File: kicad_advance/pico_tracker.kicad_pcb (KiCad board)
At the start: 2 copper layers, 92.9 x 125.4 mm, 44 parts, among them J1 MIDI_OUT, J10 DclassAMP, J11 CODEC_DIG, J12 CODEC_ANA, J13 LINE_IN, J14 PHONES, J15 MIC_MODULE, J16 FUEL_GAUGE, J2 MIDI_IN, J3 MIDI_IN_A_B_VCC, J4 MIDI_IN_A_B_DATA, J5 MIDI_OUT_A_B_VCC, J6 MIDI_OUT_A_B_DATA, J7 DISPLAY, J8 SDCARD, J9 KILL_SWITCH, SW1 SW_PG1350, SW2 SW_PG1350, SW3 SW_PG1350, SW4 SW_PG1350, SW5 SW_PG1350, SW6 SW_PG1350, SW7 SW_PG1350, SW8 SW_PG1350, SW9 SW_PG1350, U1 Pico, U2 6N138

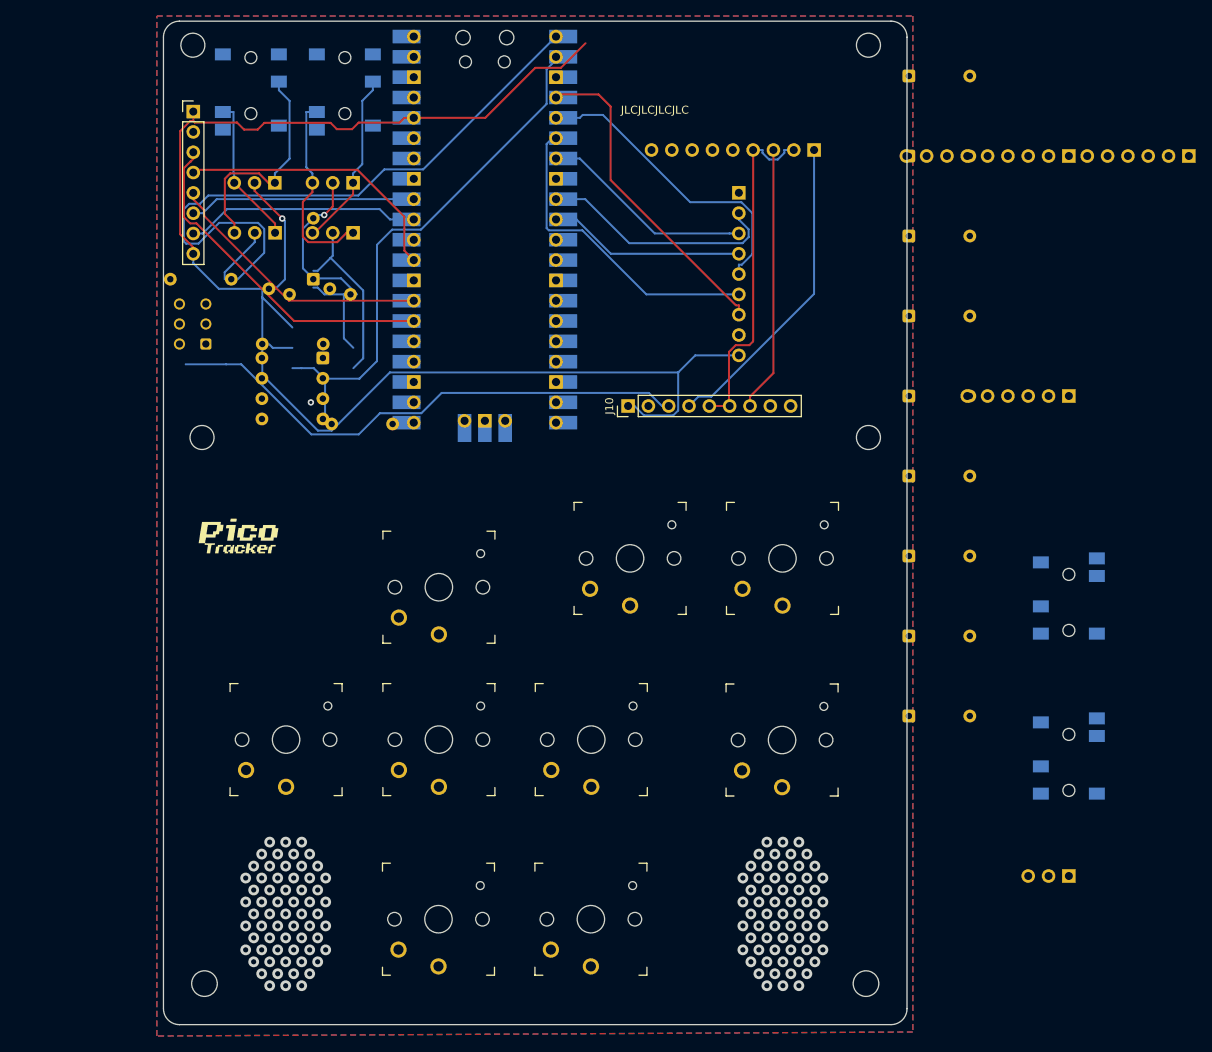
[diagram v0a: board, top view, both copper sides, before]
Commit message: Place and route the Advance-lite footprints in kicad_advance
Placement:
- All 9 matrix diodes (D2-D10) on B.Cu (back side), tucked among the
  switch rows with each cathode facing its ROW net
- Codec headers J11/J12, line-in J13, phones J14, mic J15, and
  fuel-gauge J16 placed on-board along the right edge

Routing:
- All 47 new-net connections auto-routed on a 0.2mm grid (0.25mm
  tracks, 0.25mm clearance, vias where a layer change is needed):
  COL0-2/ROW0-2 key matrix, I2S BCK/LRCK/DIN/data-in, codec MCLK,
  I2C SDA/SCL, MIC_IN, HP-amp L_AMP/R_AMP/AGND, header VCC/GND
- GND islands stitched to the pour; zones refilled

Verification:
- Total DRC count drops 528 -> 343 (refill cleared stale-fill shorts)
- No new violations on any new net; the lone new-net DRC flag
  (I2S_SDIN/VCC at U1.21/R4.2) already exists pre-routing in the
  dense MIDI/power cluster and is not caused by this work
- Switch positions, key layout, display, and MIDI jacks unchanged

Plan status section updated to reflect placed+routed state.
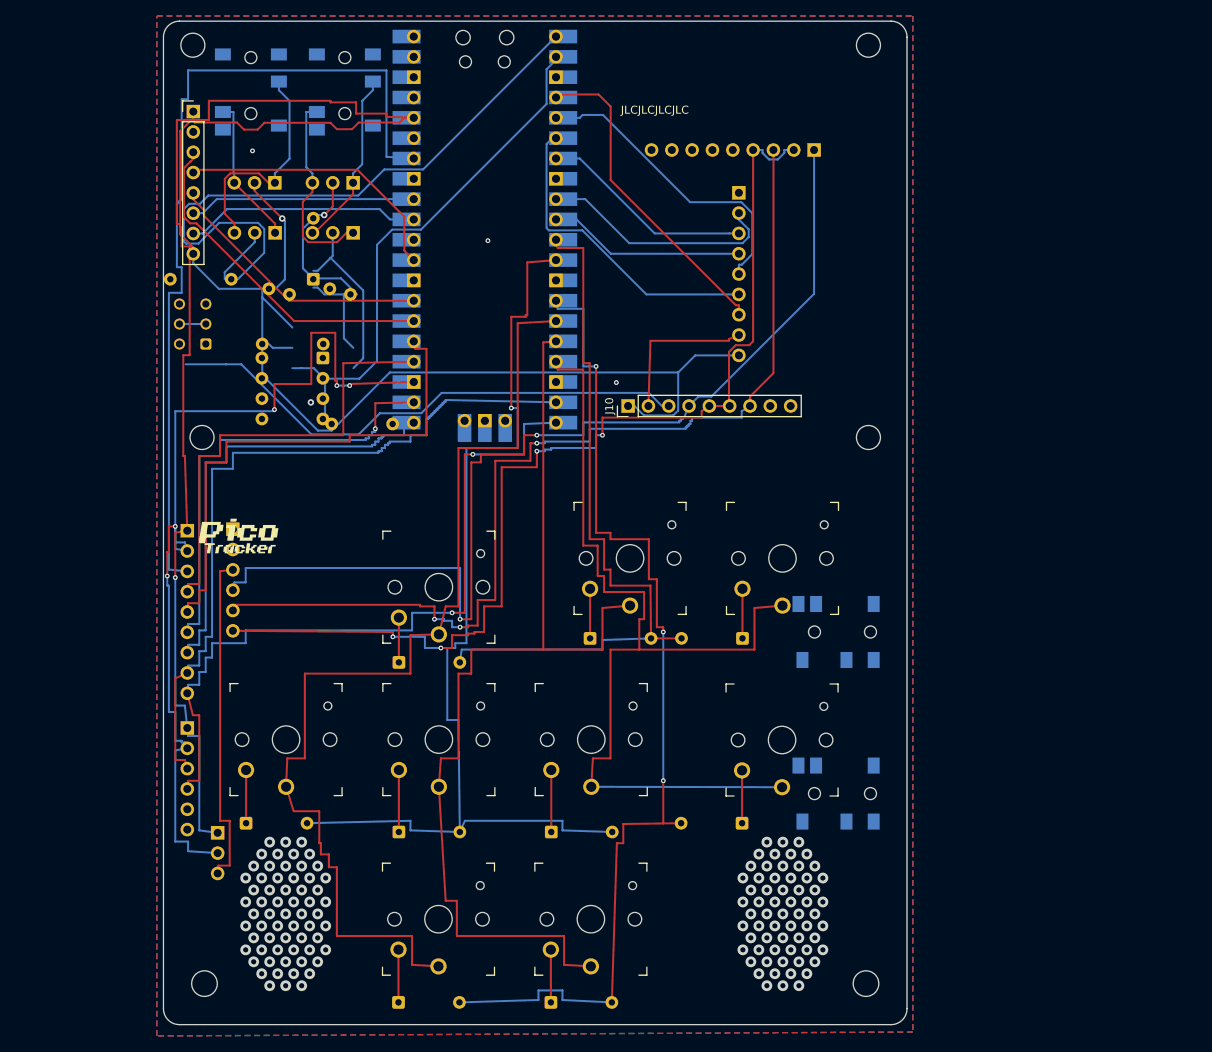
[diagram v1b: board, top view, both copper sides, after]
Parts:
- moved J16 144.2 mm to (104.8, 116.5), turned to 180 degrees
- moved D2 124.9 mm to (112.2, 128.4)
- moved J11 119.7 mm to (104.8, 91.8), turned to 180 degrees
- moved J15 106.5 mm to (108.6, 129.6), turned to 180 degrees
- moved D3 105.9 mm to (131.2, 129.5)
- moved J12 105.8 mm to (110.5, 91.7), turned to 180 degrees
- moved D6 88.0 mm to (150.2, 150.8)
- moved D4 86.9 mm to (150.3, 129.5)
- moved D9 78.5 mm to (131.2, 150.8)
- moved D5 77.1 mm to (131.2, 108.3)
- moved D7 44.7 mm to (155.2, 105.3)
- moved J13 38.2 mm to (185.9, 124.7), turned to 90 degrees
- moved J14 33.0 mm to (185.9, 104.5), turned to 90 degrees
- moved D10 24.8 mm to (174.2, 128.4), turned to 180 degrees
- moved D8 23.2 mm to (174.2, 105.3), turned to 180 degrees
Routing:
- net GND: track 0.00 -> 142.7 mm, vias 1 -> 9
- net COL0: track 0.00 -> 131.2 mm
- net ROW2: track 0.00 -> 130.4 mm, vias 0 -> 3
- net ROW1: track 0.00 -> 129.3 mm, vias 0 -> 1
- net COL1: track 0.00 -> 126.4 mm
- net COL2: track 0.00 -> 117.3 mm
- net MCLK: track 0.00 -> 107.3 mm
- net VCC: track 179.3 -> 285.6 mm, vias 0 -> 1
- net R_AMP: track 33.2 -> 128.4 mm, vias 0 -> 3
- net SDA: track 0.00 -> 94.3 mm
- net SCL: track 0.00 -> 93.9 mm, vias 0 -> 2
- net L_AMP: track 39.4 -> 131.6 mm, vias 0 -> 2
- net ROW0: track 0.00 -> 91.8 mm
- net AGND: track 44.5 -> 135.8 mm, vias 0 -> 4
- net LRCK: track 0.00 -> 65.1 mm
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
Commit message: Remove stray REF1 amp header and re-route amp nets
REF1 was an orphan footprint (a 1x9 SMD pin header on the back, upper
right) with no schematic symbol - a leftover in the original board that
tapped the class-D amp nets (L_AMP/R_AMP/AGND) in parallel with J10.

- Delete the REF1 footprint and its now-dangling feed traces
- Re-route L_AMP (J10.4<->J12.4), R_AMP (J10.7<->J12.5) and AGND
  (J12.6<->J10.5) among their real pads so nothing is left floating
- Clean up leftover AGND stub fragments near J10; refill zones

All amp-net pads remain connected (no L_AMP/R_AMP/AGND unconnected
items). Total DRC drops from 206 to 185 (REF1's courtyard/footprint
mismatch violations removed). Kept G1 (the silkscreen logo, legitimately
board-only); the SW1-9 empty footprint paths are a pre-existing quirk in
the original project and were left as-is.
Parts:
- removed REF1: PinHeader_1x09_P2.54mm_Vertical_SMD_Pin1Left, Connector_PinHeader_2.54mm:PinHeader_1x09_P2.54mm_Vertical
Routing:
- net AGND: track 135.8 -> 193.5 mm, vias 4 -> 8
- net L_AMP: track 131.6 -> 92.5 mm
- net R_AMP: track 128.4 -> 95.4 mm

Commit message: Advance-lite: widen codec header J12 to 1x9, reposition for ES8388 module mate
- J12 CODEC_ANA 6->9 pins (schematic); pins 7-9 carry the module line-out
  (LINEOUT_L/R/GND), unconnected on the mainboard.
- Move J12 on the PCB to (84.24, 91.84) so J11/J12 are 20.56mm apart, matching
  the ES8388 breakout module's two 1x9 edge headers (Digital-right/Analog-left).
- Add ES8388 module plan + schematic walkthrough docs.

Note: run Update PCB from Schematic to finalize J12's 6->9 footprint swap.
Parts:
- moved J12 26.3 mm to (84.2, 91.8)
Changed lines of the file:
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@@
 	(footprint "PinHeader_1x06_P2.54mm_Vertical"
 		(layer "B.Cu")
-		(at 110.5 91.65 180)
+		(at 84.24 91.84 180)
 		(descr "Through hole straight pin header, 1x06, 2.54mm pitch, single row")
 		(tags "Through hole pin header THT 1x06 2.54mm single row")
